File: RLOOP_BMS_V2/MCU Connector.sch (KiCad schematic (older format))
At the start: 1 part, among them J1 CONN_02X07

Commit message: footprint and layout work WIP
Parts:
- J1: footprint (none) -> Pin_Headers:Pin_Header_Straight_2x07_Pitch2.54mm_SMD
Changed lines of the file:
@@
 F 0 "J1" H 4850 3900 50  0000 C CNN
 F 1 "CONN_02X07" V 4850 3500 50  0000 C CNN
-F 2 "" H 4850 2300 50  0001 C CNN
+F 2 "Pin_Headers:Pin_Header_Straight_2x07_Pitch2.54mm_SMD" H 4850 2300 50  0001 C CNN
 F 3 "" H 4850 2300 50  0001 C CNN
 	1    4850 3500

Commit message: more PCB layout work
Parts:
- J1: footprint Pin_Headers:Pin_Header_Straight_2x07_Pitch2.54mm_SMD -> rLoop_Footprints:Pin_Header_Straight_2x07_Pitch2.54mm_SMD_MIRROR
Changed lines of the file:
@@
 F 0 "J1" H 4850 3900 50  0000 C CNN
 F 1 "CONN_02X07" V 4850 3500 50  0000 C CNN
-F 2 "Pin_Headers:Pin_Header_Straight_2x07_Pitch2.54mm_SMD" H 4850 2300 50  0001 C CNN
+F 2 "rLoop_Footprints:Pin_Header_Straight_2x07_Pitch2.54mm_SMD_MIRROR" H 4850 2300 50  0001 C CNN
 F 3 "" H 4850 2300 50  0001 C CNN
 	1    4850 3500

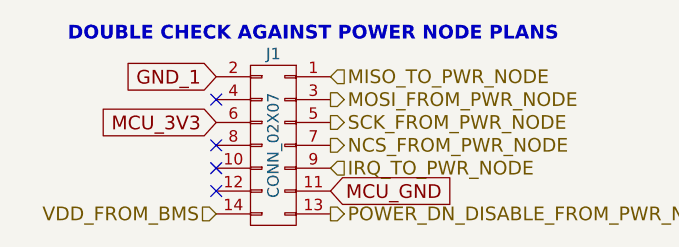
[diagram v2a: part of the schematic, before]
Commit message: More PCB work on BMS v2
lined up parts with the power node board
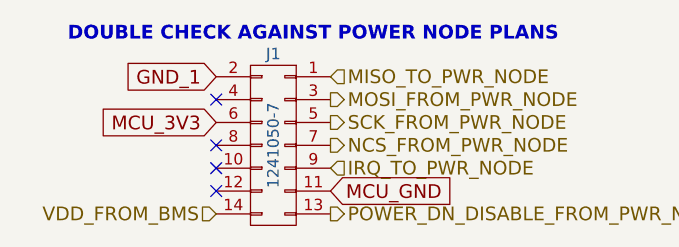
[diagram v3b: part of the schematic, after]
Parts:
- J1: value CONN_02X07 -> 1241050-7
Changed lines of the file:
@@
 P 4850 3500
 F 0 "J1" H 4850 3900 50  0000 C CNN
-F 1 "CONN_02X07" V 4850 3500 50  0000 C CNN
+F 1 "1241050-7" V 4850 3500 50  0000 C CNN
 F 2 "rLoop_Footprints:Pin_Header_Straight_2x07_Pitch2.54mm_SMD_MIRROR" H 4850 2300 50  0001 C CNN
 F 3 "" H 4850 2300 50  0001 C CNN

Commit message: more WIP
TODO:
Fix pin 50
ground planes
figure out GND_2 weirdness
fix optoisolator 3d model
bq IC 3d model
triple check everything
BOM
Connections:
- net 1_WIRE: now reaches J1.12 (P12)
- no-connect marks 4 -> 3
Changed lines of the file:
@@
 	-1   0    0    -1
 $EndComp
-NoConn ~ 4600 3700
 NoConn ~ 4600 3600
 Text GLabel 4600 3200 0    60   Input ~ 0
@@
 NoConn ~ 4600 3300
 NoConn ~ 4600 3500
+Text GLabel 4600 3700 0    60   Input ~ 0
+1_WIRE
+Wire Wire Line
+	4600 3700 4600 3700
 $EndSCHEMATC

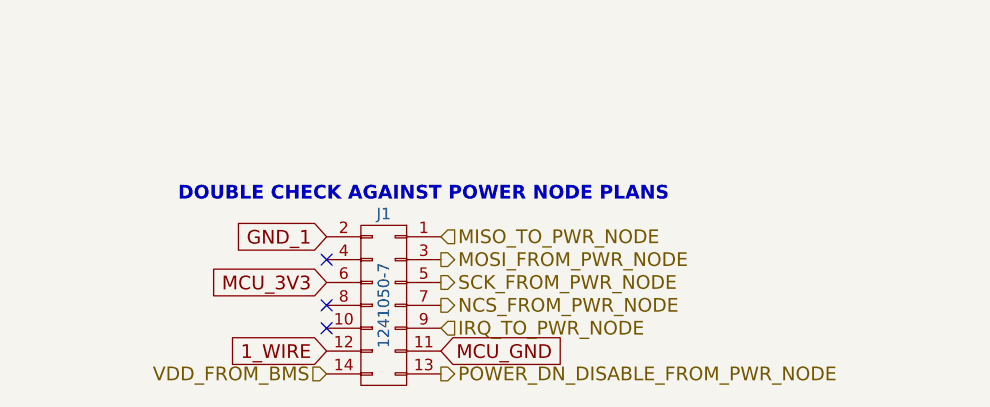
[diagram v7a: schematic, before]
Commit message: More WIP
Added connector for 1-Wire sensors if we want to put some sensors on the
heat-sinks. Just need to double check everything with the 3d-models.
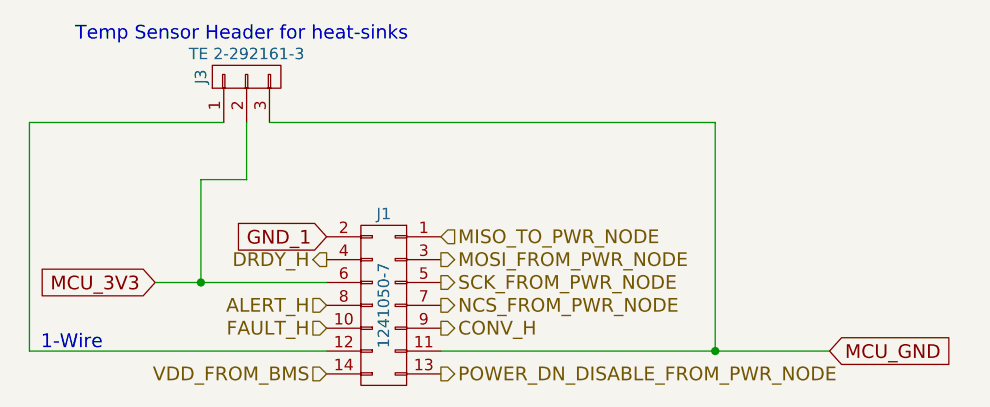
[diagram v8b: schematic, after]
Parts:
- added J3: TE 2-292161-3, Pin_Headers:Pin_Header_Straight_1x03_Pitch2.00mm, symbol CONN_01X03
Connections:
- net MCU_3V3: now also J3.2 (P2)
- net MCU_GND: now also J3.3 (P3)
- net FAULT_H: now reaches J1.10 (P10)
- net DRDY_H: now reaches J1.4 (P4)
- net ALERT_H: now reaches J1.8 (P8)
- net 1_WIRE: no longer names the net of J1.12 (P12)
- net 1_WIRE: now also J3.1 (P1)
- net IRQ_TO_PWR_NODE renamed CONV_H
- no-connect marks 3 -> 0
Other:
- note added: "1-Wire"
- note added: "Temp Sensor Header for heat-sinks"
- note removed: "DOUBLE CHECK AGAINST POWER NODE PLANS"
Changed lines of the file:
@@
 EESchema Schematic File Version 2
+LIBS:rLoop BMS v2-rescue
 LIBS:power
 LIBS:device
@@
 Comment4 ""
 $EndDescr
-Text HLabel 5100 3600 2    60   Input ~ 0
-IRQ_TO_PWR_NODE
+Text HLabel 5100 3600 2    60   Output ~ 0
+CONV_H
 Text HLabel 5100 3200 2    60   Input ~ 0
 MISO_TO_PWR_NODE
@@
 Text HLabel 5100 3800 2    60   Output ~ 0
 POWER_DN_DISABLE_FROM_PWR_NODE
-Text Notes 3950 3050 0    60   ~ 12
-DOUBLE CHECK AGAINST POWER NODE PLANS
 Text HLabel 4600 3800 0    60   Input ~ 0
 VDD_FROM_BMS
-Text GLabel 4600 3400 0    60   Input ~ 0
+Text GLabel 3850 3400 0    60   Input ~ 0
 MCU_3V3
-Text GLabel 5100 3700 2    60   Input ~ 0
+Text GLabel 6800 3700 2    60   Input ~ 0
 MCU_GND
 $Comp
@@
 	-1   0    0    -1
 $EndComp
-NoConn ~ 4600 3600
 Text GLabel 4600 3200 0    60   Input ~ 0
 GND_1
-NoConn ~ 4600 3300
-NoConn ~ 4600 3500
-Text GLabel 4600 3700 0    60   Input ~ 0
-1_WIRE
 Wire Wire Line
-	4600 3700 4600 3700
+	3300 3700 4600 3700
+Text HLabel 4600 3600 0    60   Input ~ 0
+FAULT_H
+Text HLabel 4600 3500 0    60   Input ~ 0
+ALERT_H
+Text HLabel 4600 3300 0    60   Output ~ 0
+DRDY_H
+Wire Wire Line
+	3300 3700 3300 2700
+Wire Wire Line
+	3300 2700 4150 2700
+Wire Wire Line
+	6800 3700 5100 3700
+Wire Wire Line
+	3850 3400 4600 3400
+$Comp
+L CONN_01X03 J3
+U 1 1 594AAEB6
+P 4250 2500
+F 0 "J3" H 4250 2700 50  0000 C CNN
+F 1 "TE 2-292161-3" V 4350 2500 50  0000 C CNN
+F 2 "Pin_Headers:Pin_Header_Straight_1x03_Pitch2.00mm" H 4250 2500 50  0001 C CNN
+F 3 "" H 4250 2500 50  0001 C CNN
+	1    4250 2500
+	0    -1   -1   0
+$EndComp
+Wire Wire Line
+	4250 2700 4250 2950
+Wire Wire Line
+	4250 2950 4050 2950
+Wire Wire Line
+	4050 2950 4050 3400
+Connection ~ 4050 3400
+Wire Wire Line
+	4350 2700 6300 2700
+Wire Wire Line
+	6300 2700 6300 3700
+Connection ~ 6300 3700
+Text Notes 3350 3700 0    60   ~ 0
+1-Wire
+Text Notes 3500 2350 0    60   ~ 0
+Temp Sensor Header for heat-sinks
 $EndSCHEMATC
